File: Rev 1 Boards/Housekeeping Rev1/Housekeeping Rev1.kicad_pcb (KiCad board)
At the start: 2 copper layers, 127 x 98 mm, 64 parts, among them J1 Conn_01x02_Socket, J2 Conn_01x02_Socket, J3 Conn_01x02_Socket, J4 Conn_01x02_Socket, J5 Conn_01x02_Socket, J6 Conn_01x02_Socket, U1 MC34063A, U2 MC34063A, U3 MC34063A, U4 MC34063A

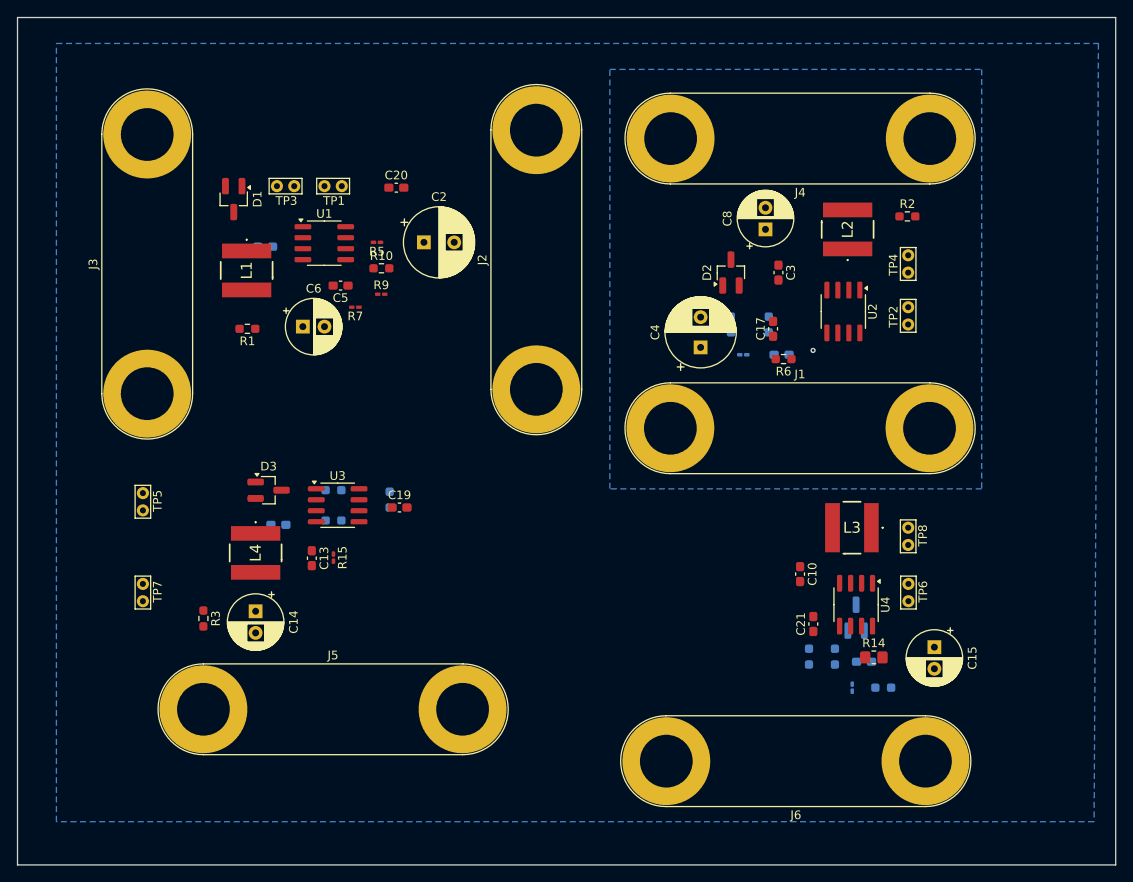
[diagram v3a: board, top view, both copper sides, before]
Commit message: Created preliminary layout for Housekeeping PCB with traces added. Still needs review + connection of nets to ground fills.
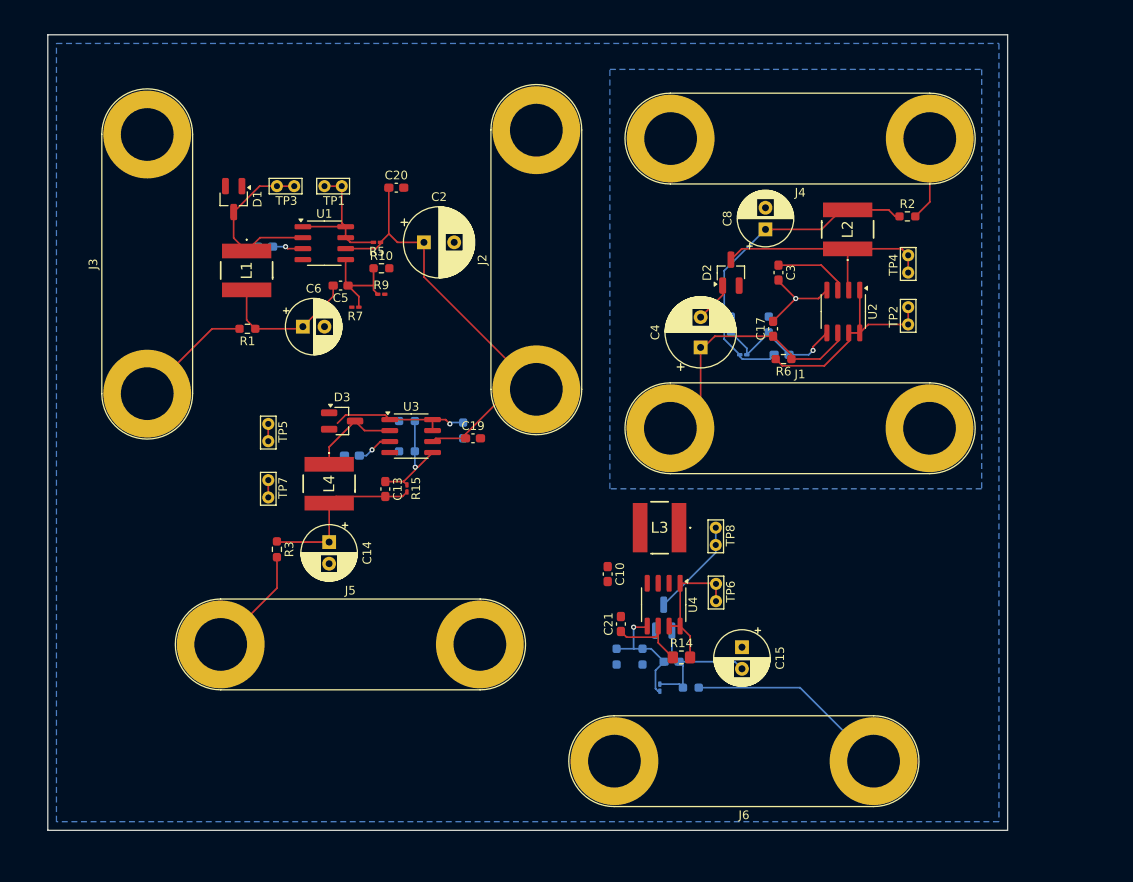
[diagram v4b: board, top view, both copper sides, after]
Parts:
- moved C10 22.2 mm to (211.2, 81.9)
- moved C15 22.2 mm to (226.8, 90.3)
- moved C16 22.2 mm to (218.6, 92.0)
- moved C21 22.2 mm to (212.8, 87.6)
- moved D4 22.2 mm to (217.7, 86.9)
- moved L3 22.2 mm to (217.2, 76.5)
- moved R14 22.2 mm to (219.8, 91.5)
- moved R16 22.2 mm to (217.3, 95.0)
- moved R19 22.2 mm to (215.3, 91.4)
- moved R20 22.2 mm to (212.3, 91.4)
- moved R4 22.2 mm to (220.9, 95.0)
- moved TP6 22.2 mm to (223.8, 85.0)
- moved TP8 22.2 mm to (223.8, 78.5)
- moved U4 22.2 mm to (217.7, 85.4)
- moved TP7 18.8 mm to (172.0, 73.0)
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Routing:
- net /+24_{MiniPC}: track 0.00 -> 65.8 mm
- net +3.3VA: track 0.00 -> 38.5 mm
- net +24V: track 0.00 -> 30.4 mm
- net Net-(D2-K): track 0.00 -> 28.2 mm
- net Net-(U2-DC): track 0.00 -> 25.1 mm
- net /-3V3bR: track 0.00 -> 23.7 mm
- net Net-(D1-K): track 0.00 -> 20.5 mm
- net +5V: track 0.00 -> 20.1 mm
- net Net-(U3-DC): track 0.00 -> 18.8 mm, vias 0 -> 1
- net -3V3: track 0.00 -> 17.6 mm
- net +3V3: track 0.00 -> 16.7 mm
- net Net-(U1-DC): track 0.00 -> 16.5 mm
- net Net-(U4-DC): track 0.00 -> 16.5 mm
- net Net-(U2-COMP-): track 0.00 -> 16.2 mm
- net GNDPWR: track 0.00 -> 15.4 mm, vias 0 -> 1
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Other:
- board size 127 x 98 mm -> 111 x 92 mm

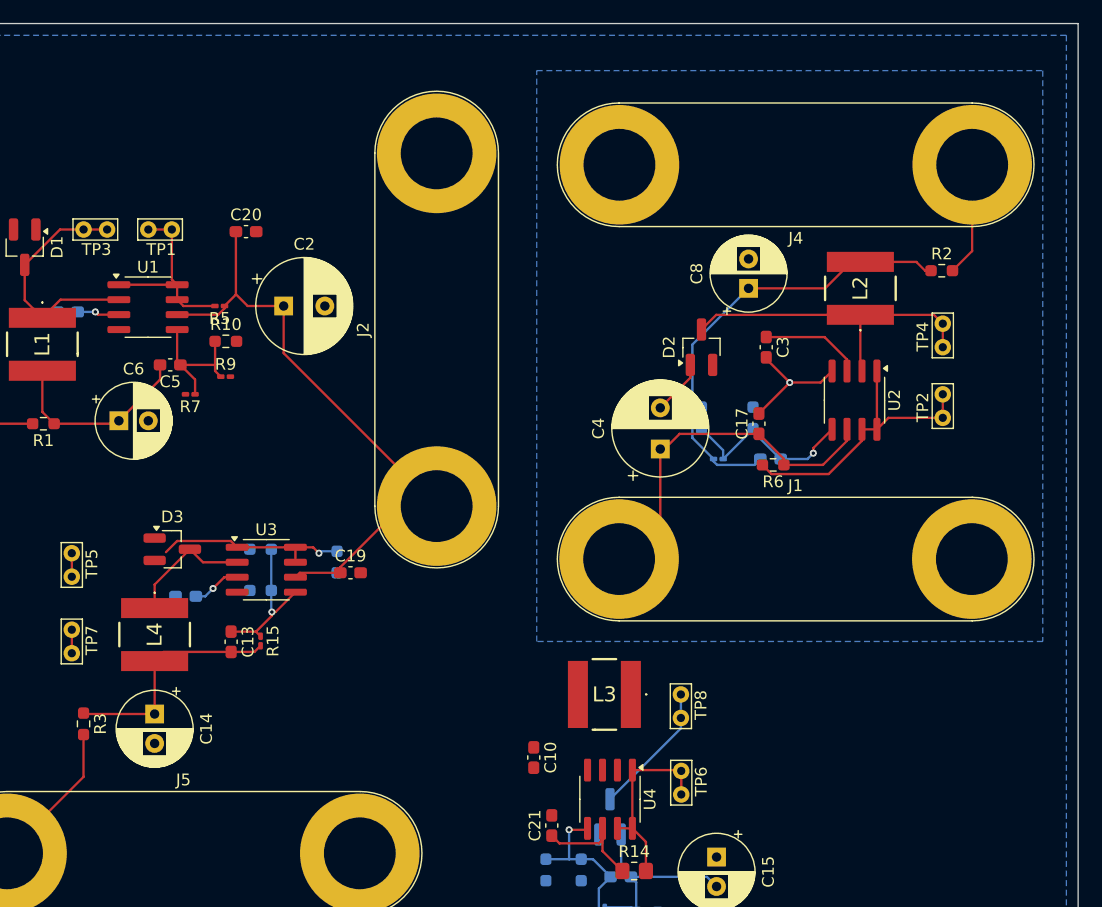
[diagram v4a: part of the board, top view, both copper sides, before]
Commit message: added traces and pours for housekeeping pcb layout
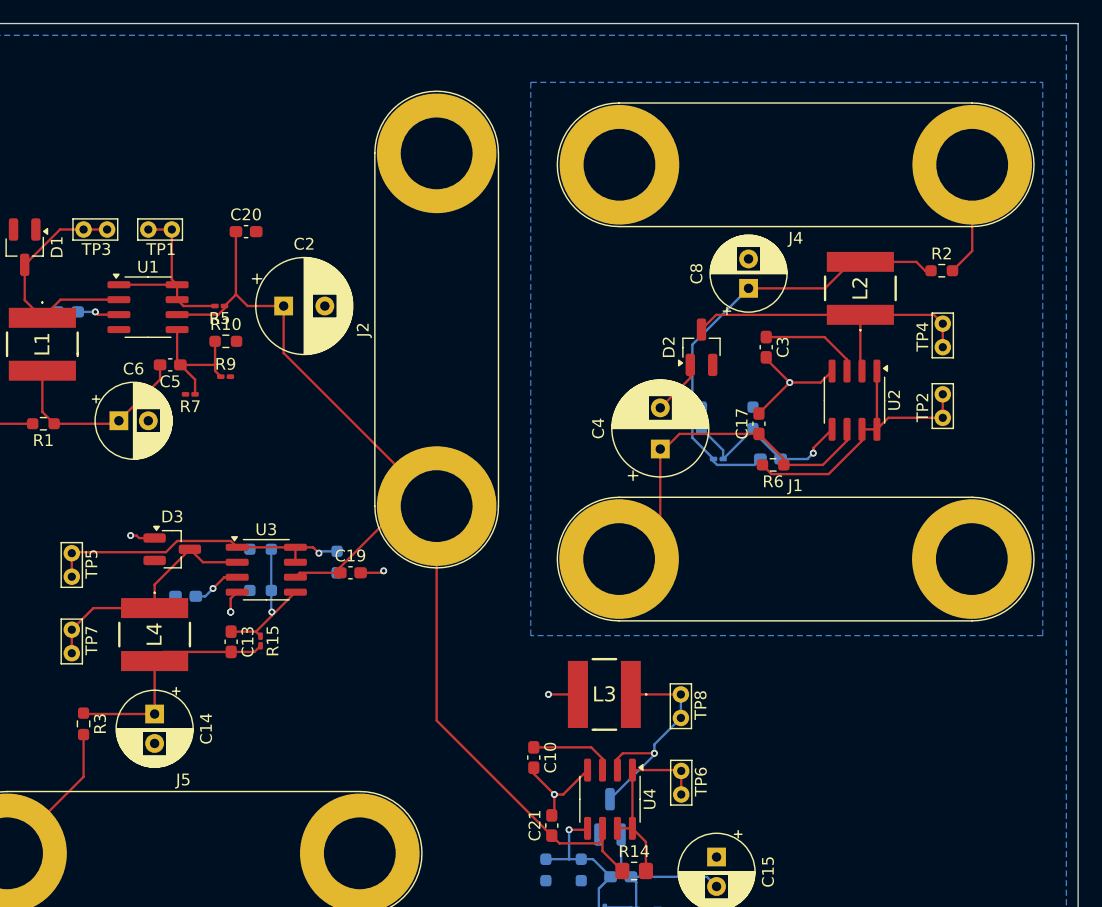
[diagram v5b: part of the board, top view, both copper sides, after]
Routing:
- net /+24_{MiniPC}: track 65.8 -> 97.9 mm
- net GND: track 0.00 -> 17.1 mm, vias 0 -> 6
- net Net-(D4-K): track 11.4 -> 20.0 mm, vias 0 -> 1
- net Net-(U3-DC): track 18.8 -> 26.7 mm
- net Net-(D3-K): track 13.2 -> 21.0 mm
- net Net-(U4-CT): track 0.00 -> 7.21 mm

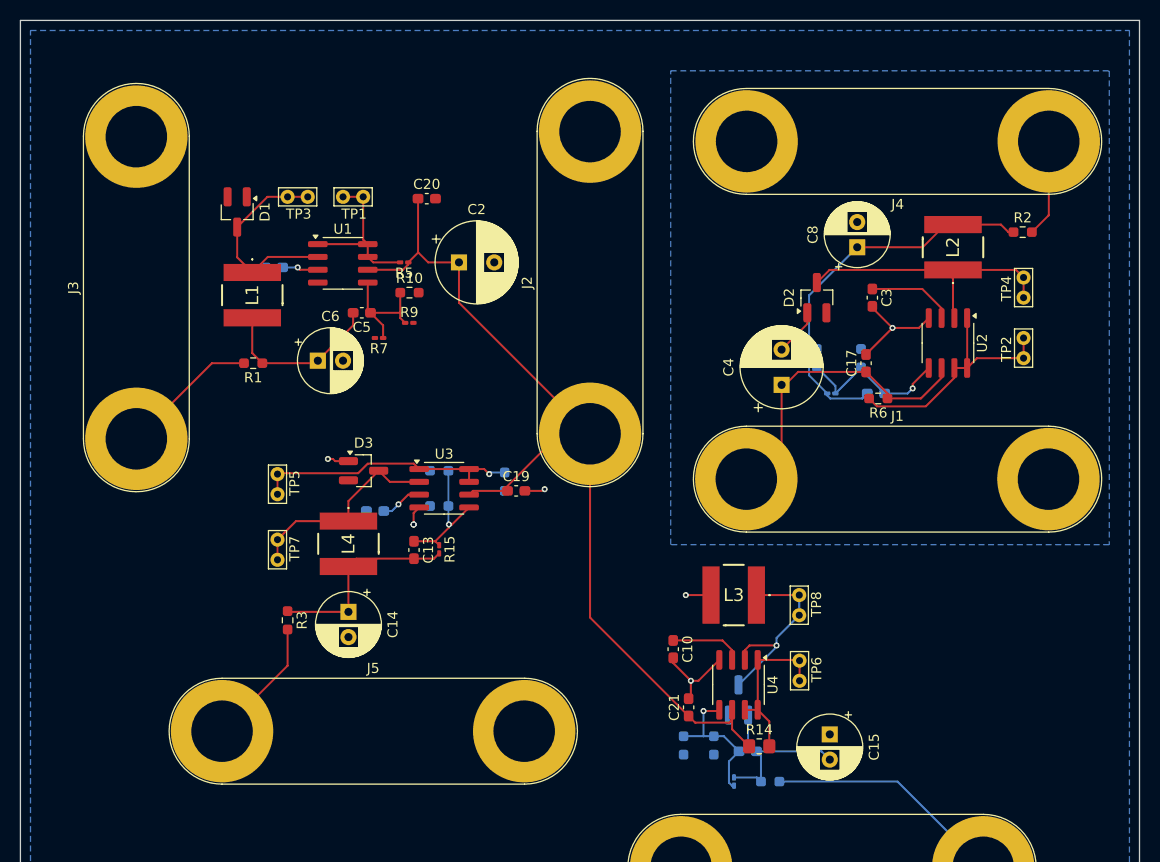
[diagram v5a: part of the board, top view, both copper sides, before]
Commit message: Updated Housekeeping PCB layout after review with Jed
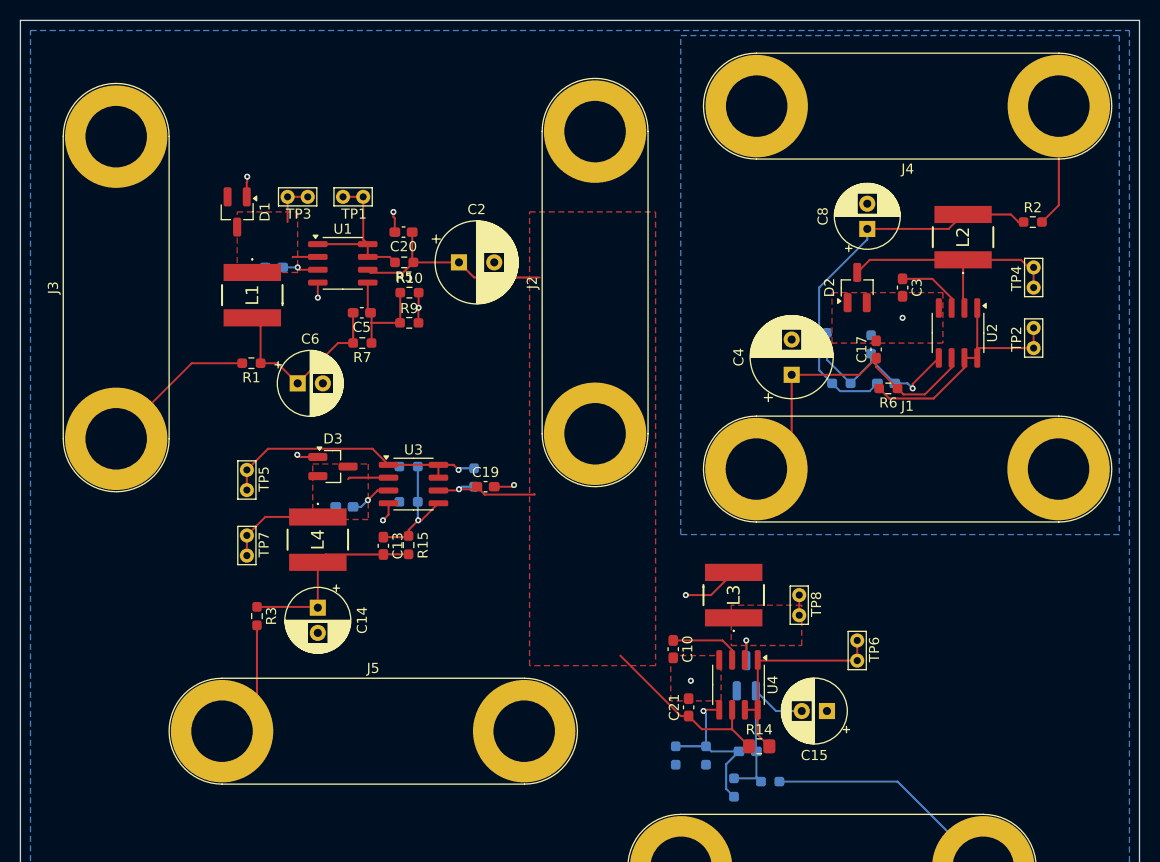
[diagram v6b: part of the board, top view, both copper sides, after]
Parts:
- R15, R16, R5, R7, R8, R9: footprint Resistor_SMD:R_0201_0603Metric_Pad0.64x0.40mm_HandSolder -> Resistor_SMD:R_0603_1608Metric_Pad0.98x0.95mm_HandSolder
- moved TP6 6.06 mm to (229.5, 83.0)
- moved D2 4.12 mm to (229.5, 46.0)
- moved C20 4.04 mm to (184.5, 40.5), turned to 180 degrees
- moved J4 3.64 mm to (249.5, 28.0)
- moved C3 3.16 mm to (234.0, 46.0)
- moved C19 3.07 mm to (192.6, 65.8)
- moved C9 3.07 mm to (178.6, 67.8)
- moved C13 3.07 mm to (182.5, 71.6)
- moved C14 3.07 mm to (176.0, 77.8)
- moved D3 3.07 mm to (177.5, 63.8)
- moved L4 3.07 mm to (176.0, 71.0)
- moved R17 3.07 mm to (185.0, 63.8)
- moved R18 3.07 mm to (185.0, 67.2)
- moved R3 3.07 mm to (170.0, 78.6)
- moved TP5 3.07 mm to (169.0, 66.1)
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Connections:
- net Net-(D1-K) renamed /Housekeeping Power Supplies/3V3_SW
- net Net-(D2-K) renamed /Housekeeping Power Supplies/3V3A_SW
- net Net-(D3-K) renamed /Housekeeping Power Supplies/5V_SW
- net Net-(D4-K) renamed /Housekeeping Power Supplies/-3V3_SW
- net Net-(U1-COMP-) renamed /Housekeeping Power Supplies/3V3_COMP
- net Net-(U1-CT) renamed /Housekeeping Power Supplies/3V3_CT
- net Net-(U1-DC) renamed /Housekeeping Power Supplies/3V3_VC
- net Net-(U2-COMP-) renamed /Housekeeping Power Supplies/3V3A_COMP
- net Net-(U2-CT) renamed /Housekeeping Power Supplies/3V3A_CT
- net Net-(U2-DC) renamed /Housekeeping Power Supplies/3V3A_VC
- net Net-(U3-COMP-) renamed /Housekeeping Power Supplies/5V_COMP
- net Net-(U3-CT) renamed /Housekeeping Power Supplies/5V_CT
- net Net-(U3-DC) renamed /Housekeeping Power Supplies/5V_VC
- net Net-(U4-COMP-) renamed /Housekeeping Power Supplies/-3V3_COMP
- net Net-(U4-CT) renamed /Housekeeping Power Supplies/-3V3_CT
- net Net-(U4-DC) renamed /Housekeeping Power Supplies/-3V3_VC
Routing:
- net /+24_{MiniPC}: track 97.9 -> 51.3 mm, vias 0 -> 1
- net GNDPWR: track 15.4 -> 0.35 mm
- net /Housekeeping Power Supplies/-3V3_SW: track 20.0 -> 6.34 mm
- net /Housekeeping Power Supplies/3V3_SW: track 20.5 -> 7.02 mm
- net /Housekeeping Power Supplies/5V_SW: track 21.0 -> 13.9 mm
- net /Housekeeping Power Supplies/-3V3_VC: track 16.5 -> 22.2 mm
- net GND: track 17.1 -> 20.3 mm, vias 6 -> 9
- net /Housekeeping Power Supplies/3V3A_SW: track 28.2 -> 25.2 mm
- net +3V3: track 16.7 -> 19.5 mm
- net /Housekeeping Power Supplies/-3V3_COMP: track 14.4 -> 17.1 mm
- net /3V3AbR: track 9.69 -> 12.2 mm
- net /Housekeeping Power Supplies/3V3A_CT: track 8.63 -> 6.63 mm
- net /3V3bR: track 13.8 -> 15.6 mm
- net /Housekeeping Power Supplies/3V3A_COMP: track 16.2 -> 17.9 mm
- net +24V: track 30.4 -> 31.4 mm
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- added copper zone on F.Cu, net /+24_{MiniPC}
- added copper zone on F.Cu, net /Housekeeping Power Supplies/-3V3_SW
- added copper zone on F.Cu, net /Housekeeping Power Supplies/3V3_SW
- added copper zone on F.Cu, net /Housekeeping Power Supplies/5V_SW
- added copper zone on F.Cu, net GND
- added copper zone on F.Cu, net GNDPWR

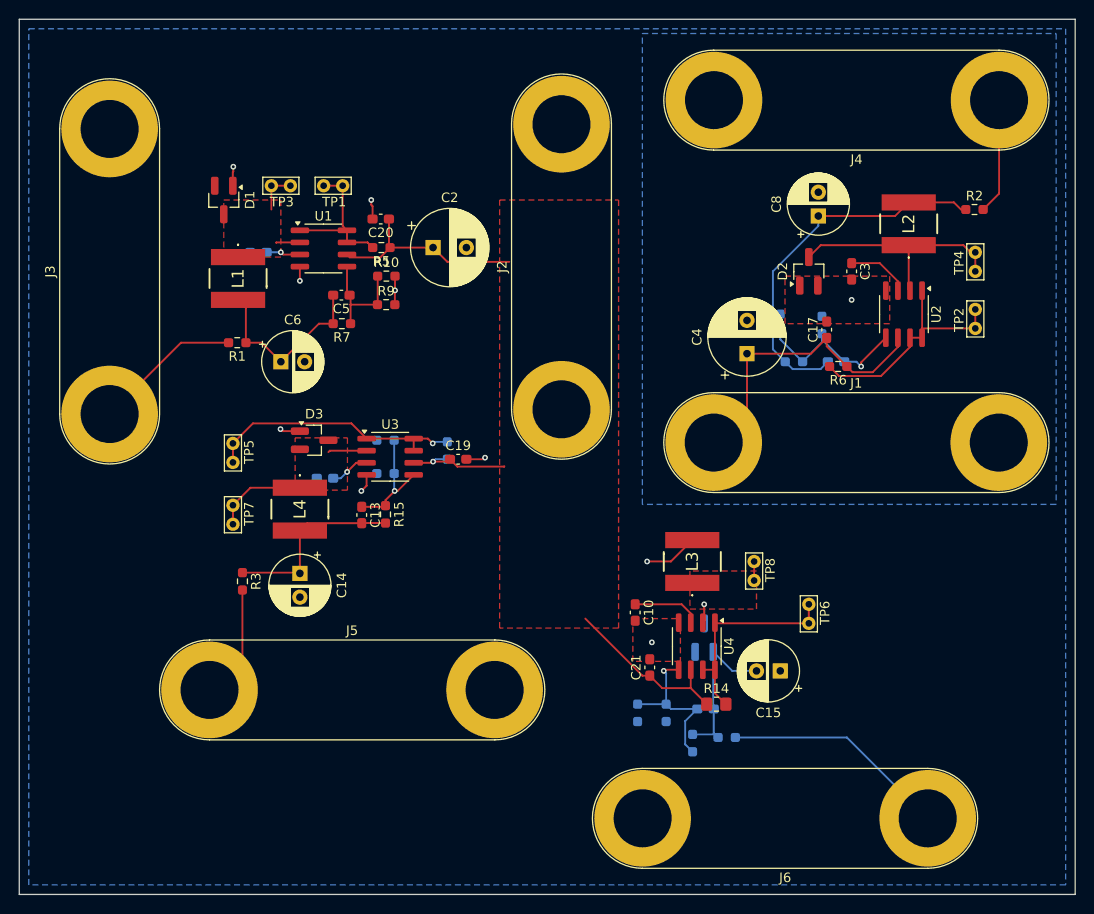
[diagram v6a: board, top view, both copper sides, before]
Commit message: Changed fill types for SW nets and added silkscreen labels for banana connectors
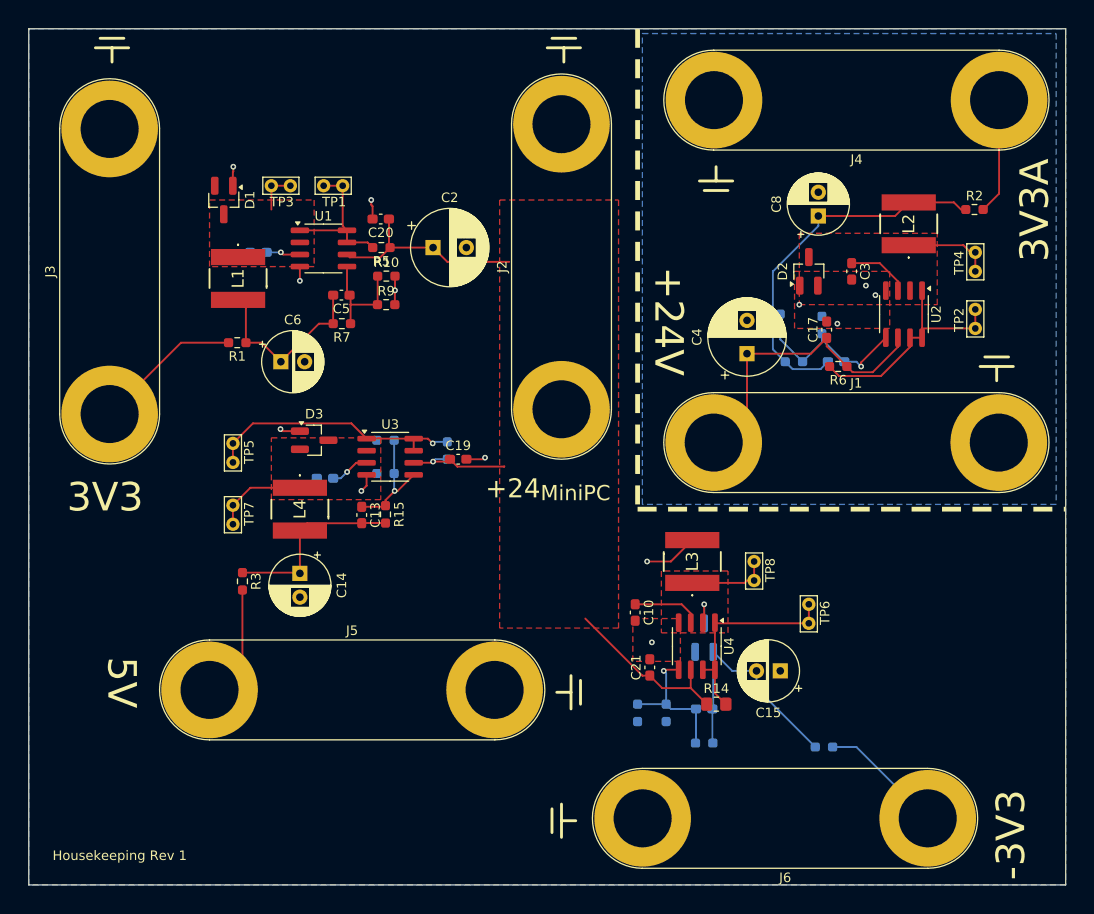
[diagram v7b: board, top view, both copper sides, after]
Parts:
- moved R4 10.3 mm to (231.1, 96.0)
- moved R16 1.22 mm to (218.5, 95.6), turned to 0 degrees
- moved C16 0.14 mm to (218.5, 92.0)
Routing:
- net /Housekeeping Power Supplies/3V3A_SW: track 25.2 -> 9.50 mm
- net /-3V3bR: track 23.7 -> 13.1 mm
- net -3V3: track 17.4 -> 25.5 mm
- net /Housekeeping Power Supplies/-3V3_SW: track 6.34 -> 12.9 mm
- net /Housekeeping Power Supplies/5V_SW: track 13.9 -> 9.80 mm
- net /Housekeeping Power Supplies/3V3_SW: track 7.02 -> 4.50 mm
- net /Housekeeping Power Supplies/-3V3_COMP: track 17.1 -> 15.2 mm
- net GNDPWR: vias 1 -> 4
- added copper zone on F.Cu, net /Housekeeping Power Supplies/3V3A_SW
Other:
- board size 111 x 92 mm -> 109 x 90 mm
- board text added: "+24V"
- board text added: "+24_{MiniPC}"
- board text added: "-3V3"
- board text added: "3V3"
- board text added: "3V3A"
- board text added: "5V"
- board text added: "Housekeeping Rev 1"
